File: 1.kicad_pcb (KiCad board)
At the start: 2 copper layers, 85.1 x 46.4 mm, 44 parts, among them J1 Micro_SD_Card, J10 I2C1, J11 I2C2, J12 B3..9A, J2 USB_B_Micro, J3 Conn_Power, J4 SWD, J5 Protected, J6 SPI1, J7 ADC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

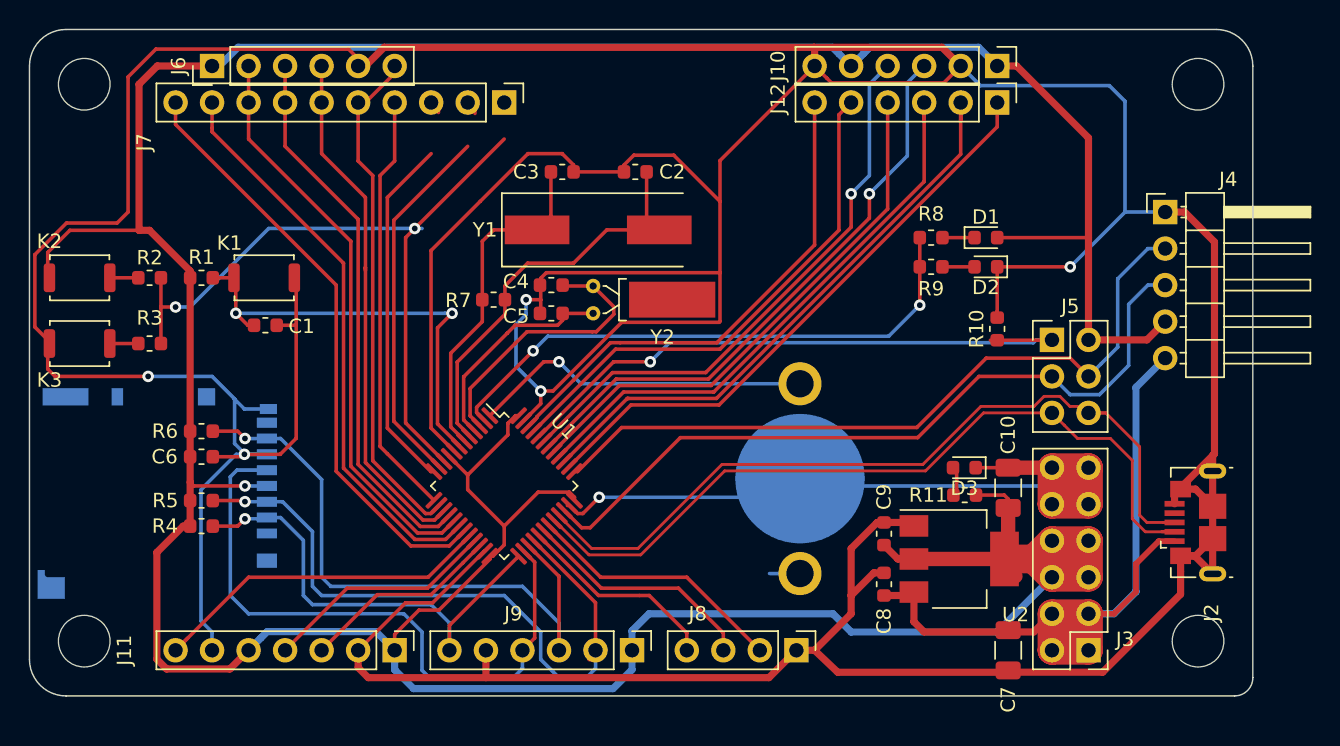
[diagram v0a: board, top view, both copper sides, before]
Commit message: operate line near edge
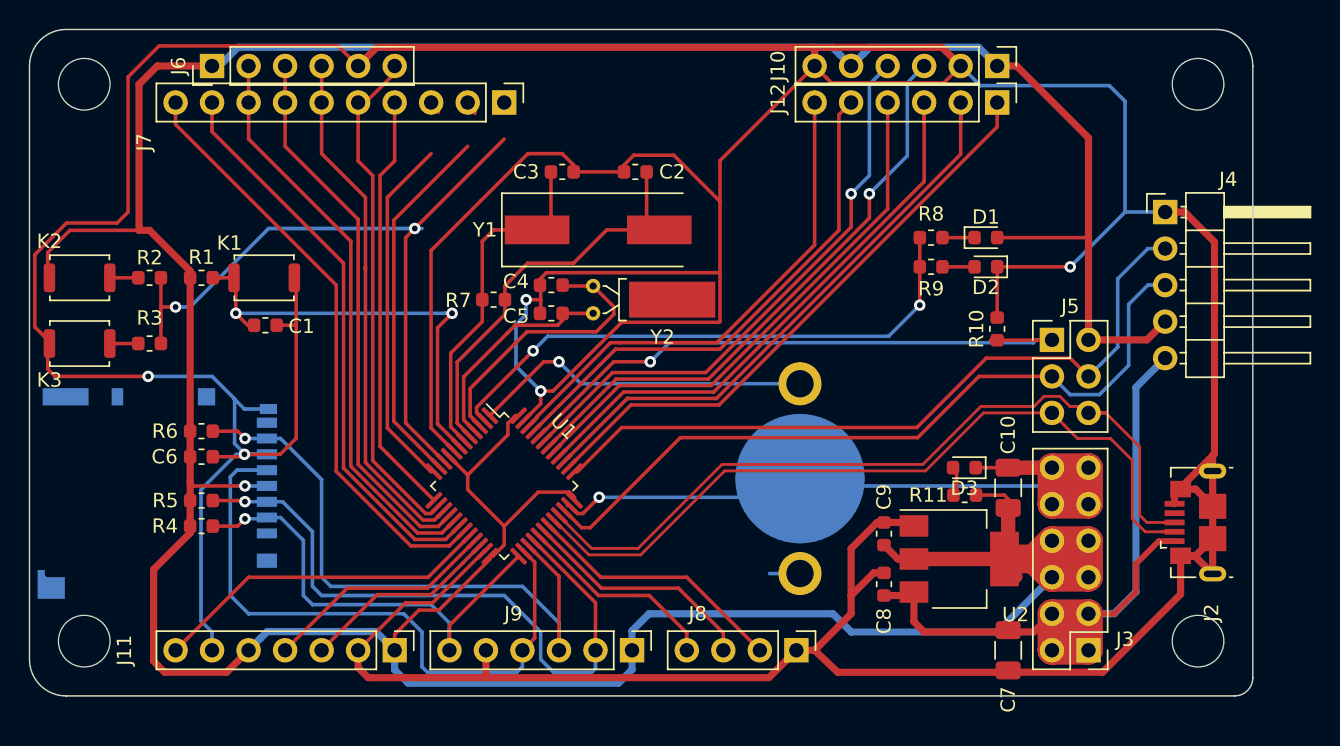
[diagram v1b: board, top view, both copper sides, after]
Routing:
- net /SD_SCLK: track 44.3 -> 43.8 mm

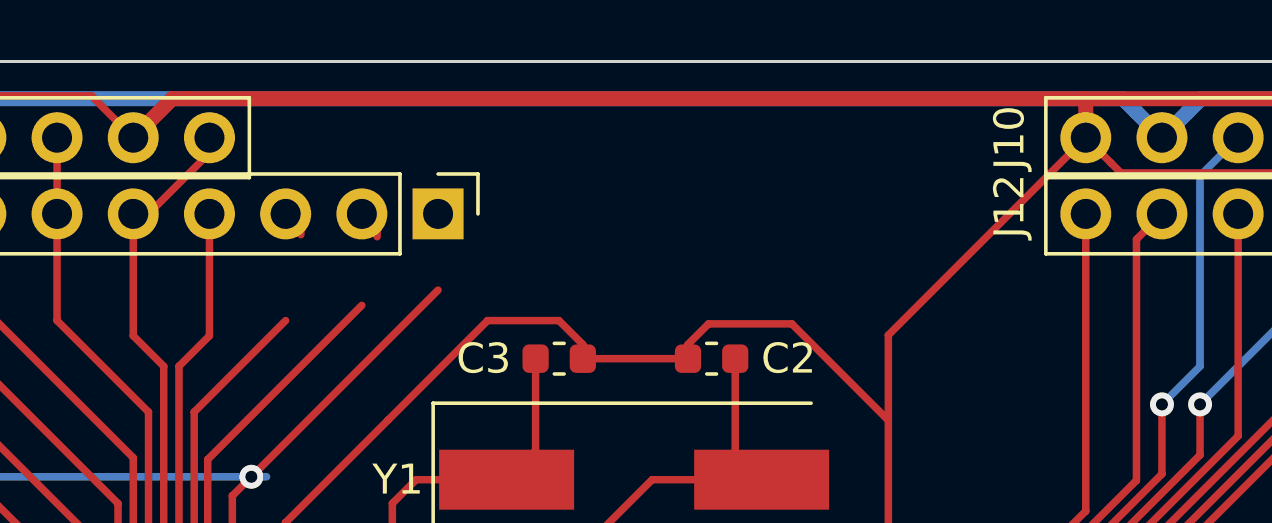
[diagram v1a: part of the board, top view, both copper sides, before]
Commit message: fix: ADC channel no connect
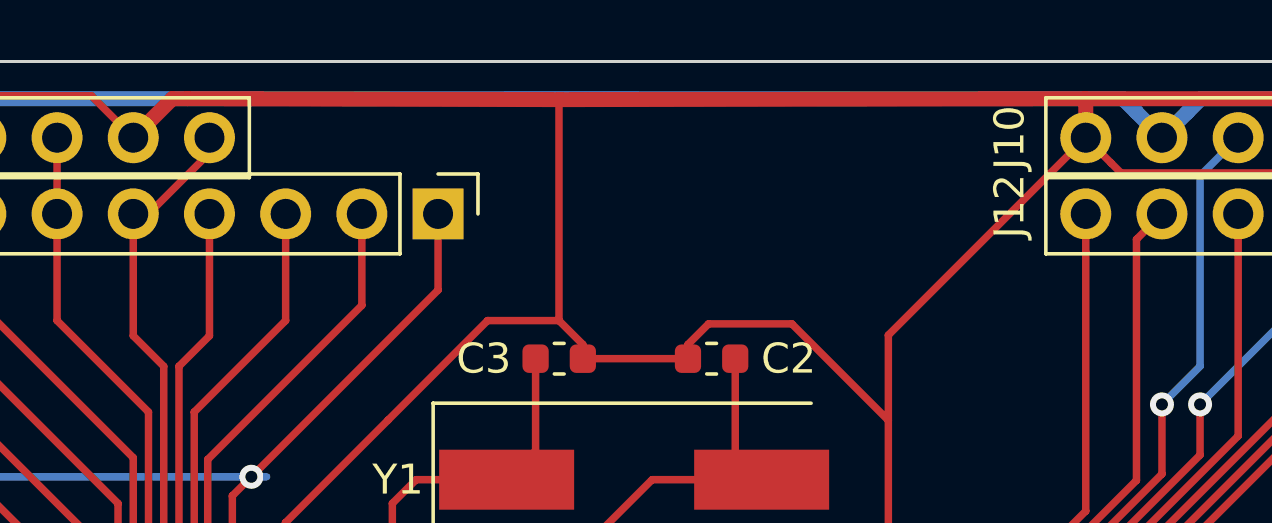
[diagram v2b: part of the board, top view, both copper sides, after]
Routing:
- net GND: track 485.7 -> 493.1 mm
- net /PA0: track 52.5 -> 55.0 mm
- net /PA2: track 26.0 -> 28.4 mm
- net /PA1: track 27.0 -> 28.7 mm
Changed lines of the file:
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@@
     (thickness 1.6)
     (drawings 27)
-    (tracks 644)
+    (tracks 648)
     (zones 0)
     (modules 44)
@@
       (effects (font (size 1 1) (thickness 0.15)))
     )
-    (fp_text value 8MHz (at 11.244 5.110244) (layer F.Fab) hide
+    (fp_text value 8MHz (at 9.212 0.030244) (layer F.Fab) hide
       (effects (font (size 1 1) (thickness 0.15)))
     )
@@
       (effects (font (size 1 1) (thickness 0.15)))
     )
-    (fp_text value 32.768k (at 5.7735 10.795) (layer F.Fab) hide
+    (fp_text value 32.768k (at 0.9475 12.104) (layer F.Fab) hide
       (effects (font (size 1 1) (thickness 0.15)))
     )
@@
     )
   )
-  (gr_text "ADCx\nCH9..0" (at 120.142 102.87) (layer Dwgs.User)
+  (gr_text "ADCx\nCH9..0" (at 120.142 109.4994) (layer Dwgs.User)
     (effects (font (size 1.5 1.5) (thickness 0.3)))
   )
@@
   (segment (start 159.989999 87.599999) (end 151.099999 87.599999) (width 0.5) (layer F.Cu) (net 7))
   (segment (start 161.29 88.9) (end 159.989999 87.599999) (width 0.5) (layer F.Cu) (net 7))
-  (segment (start 121.188001 87.599999) (end 151.099999 87.599999) (width 0.5) (layer F.Cu) (net 7))
   (segment (start 120.680001 87.599999) (end 121.188001 87.599999) (width 0.5) (layer F.Cu) (net 7))
   (segment (start 119.38 88.9) (end 120.680001 87.599999) (width 0.5) (layer F.Cu) (net 7))
@@
   (segment (start 98.298 110.49) (end 104.775 110.49) (width 0.25) (layer F.Cu) (net 7))
   (segment (start 119.38 88.9) (end 117.983 87.503) (width 0.25) (layer F.Cu) (net 7))
+  (segment (start 133.571 87.663) (end 133.604 87.63) (width 0.25) (layer F.Cu) (net 7))
+  (segment (start 133.571 94.996) (end 133.571 87.663) (width 0.25) (layer F.Cu) (net 7))
+  (segment (start 133.604 87.63) (end 151.099999 87.599999) (width 0.5) (layer F.Cu) (net 7))
+  (segment (start 121.188001 87.599999) (end 133.604 87.63) (width 0.5) (layer F.Cu) (net 7))
   (segment (start 163.83 100.838) (end 170.18 100.838) (width 0.25) (layer F.Cu) (net 8))
   (segment (start 170.18 100.838) (end 170.18 107.95) (width 0.5) (layer F.Cu) (net 8))
@@
   (segment (start 120.904 115.360664) (end 121.412 115.868664) (width 0.25) (layer F.Cu) (net 32))
   (segment (start 120.904 96.52) (end 120.904 115.360664) (width 0.25) (layer F.Cu) (net 32))
-  (segment (start 124.968 90.932) (end 124.968 92.134081) (width 0.25) (layer F.Cu) (net 33))
   (segment (start 124.46 94.996) (end 121.412 98.044) (width 0.25) (layer F.Cu) (net 33))
   (segment (start 124.439992 117.111212) (end 121.412 114.08322) (width 0.25) (layer F.Cu) (net 33))
   (segment (start 121.412 114.08322) (end 121.412 98.044) (width 0.25) (layer F.Cu) (net 33))
   (segment (start 124.652124 117.111212) (end 124.439992 117.111212) (width 0.25) (layer F.Cu) (net 33))
-  (segment (start 127.508 90.932) (end 127.508 92.202) (width 0.25) (layer F.Cu) (net 34))
+  (segment (start 124.46 91.44) (end 124.46 94.996) (width 0.25) (layer F.Cu) (net 33))
   (segment (start 121.86201 99.62599) (end 127 94.488) (width 0.25) (layer F.Cu) (net 34))
   (segment (start 121.86201 113.61399) (end 121.86201 99.62599) (width 0.25) (layer F.Cu) (net 34))
   (segment (start 125.005678 116.757658) (end 121.86201 113.61399) (width 0.25) (layer F.Cu) (net 34))
+  (segment (start 127 94.488) (end 127 91.44) (width 0.25) (layer F.Cu) (net 34))
   (segment (start 130.048 92.032) (end 130.048 90.932) (width 0.25) (layer F.Cu) (net 35))
   (segment (start 129.54 93.98) (end 123.317 100.203) (width 0.25) (layer F.Cu) (net 35))
@@
   (segment (start 122.682 113.726874) (end 122.682 100.838) (width 0.25) (layer F.Cu) (net 35))
   (segment (start 125.359231 116.404105) (end 122.682 113.726874) (width 0.25) (layer F.Cu) (net 35))
+  (segment (start 129.54 93.98) (end 129.54 91.44) (width 0.25) (layer F.Cu) (net 35))
   (segment (start 151.13 92.71) (end 151.13 91.44) (width 0.25) (layer F.Cu) (net 36))
   (segment (start 136.931833 108.14601) (end 137.600401 108.146009) (width 0.25) (layer F.Cu) (net 36))

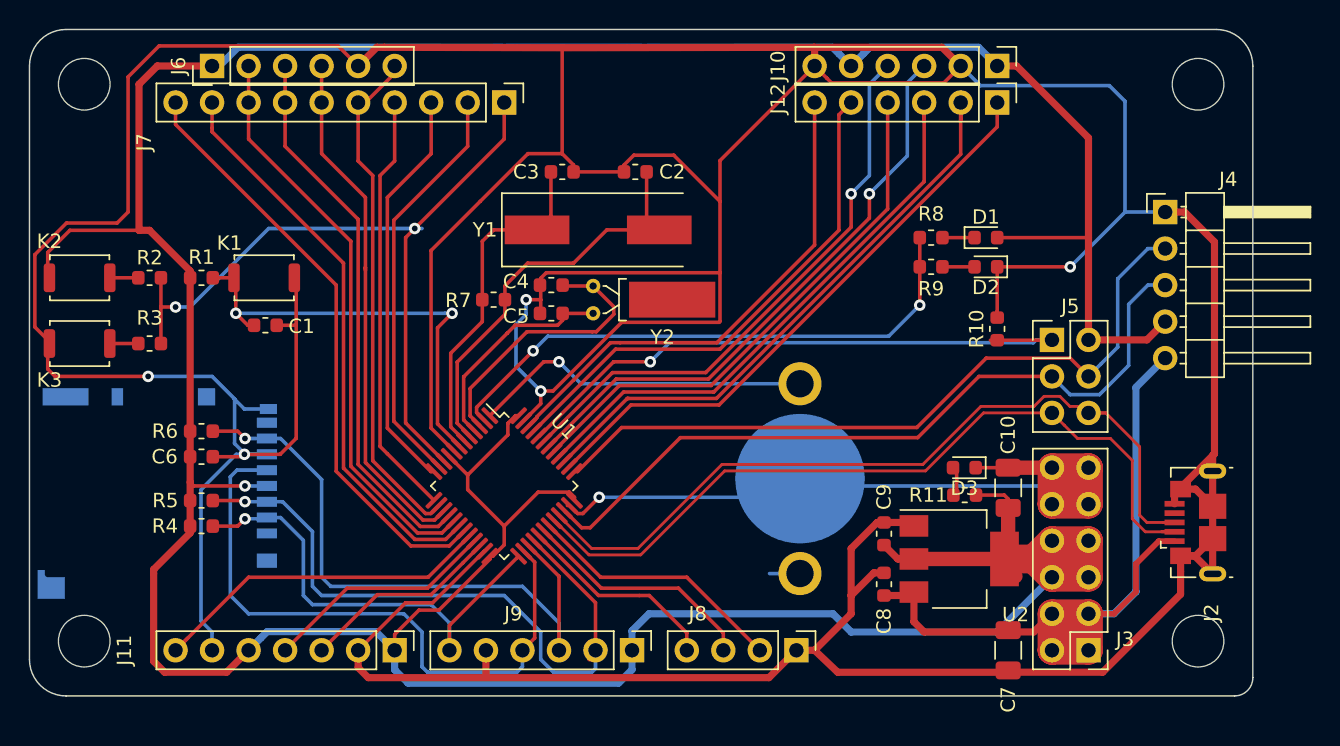
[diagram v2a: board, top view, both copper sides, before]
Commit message: label two colors
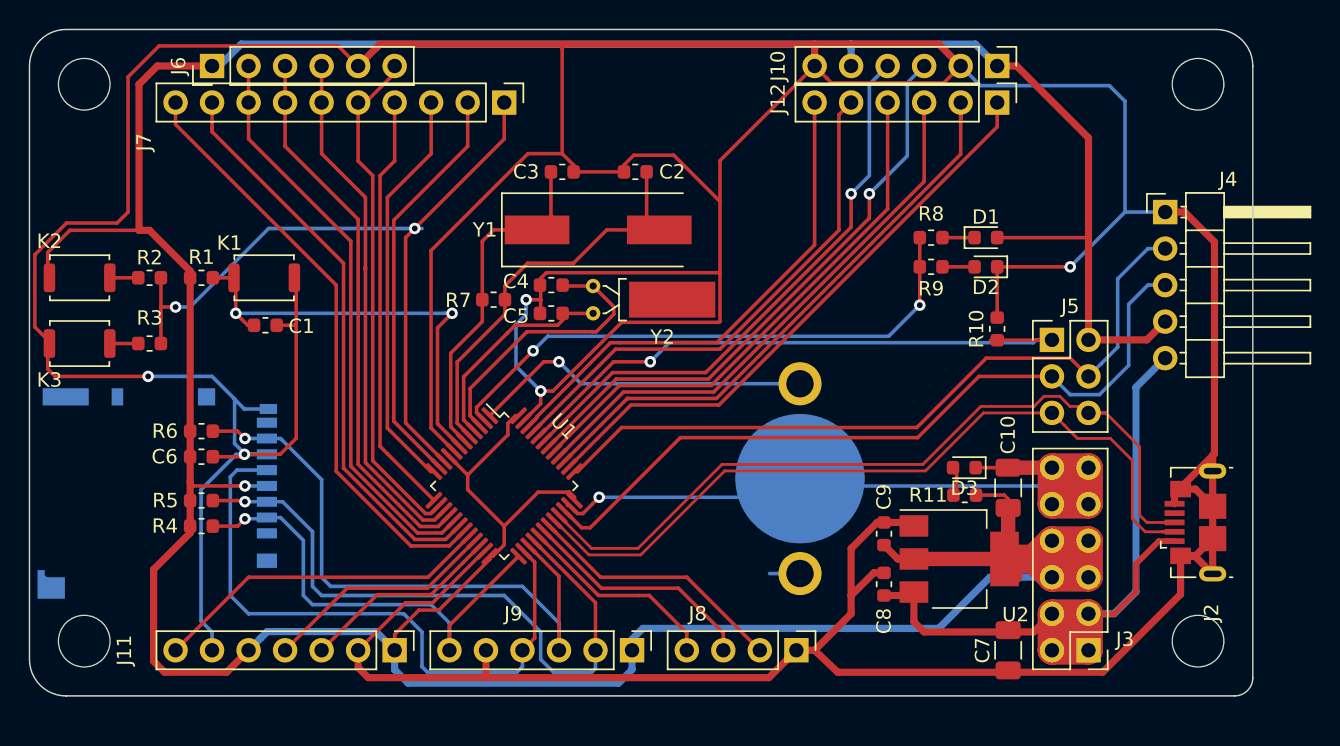
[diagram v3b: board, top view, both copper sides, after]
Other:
- board text added: "+ -"
- board text added: "- +"
- board text added: "- + SCL SDA - +"
- board text added: ". . . . SPI1"
- board text added: "2 1 2 1 TIM3 TIM4"
- board text added: "3V3 GND"
- board text added: "B11 B10 B2"
- board text added: "MOSI MISO SCK NSS"
- board text added: "OSC"
- board text added: "SDA SCL"
- board text added: "TIM4 2 1 4 3"
- board text removed: "- + SDA SCL - +"
- board text removed: "3V3 MOSI MISO SCK GND NSS"
- board text removed: "B11 B10"
- board text removed: "B2 - + SCL SDA - +"

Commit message: labels
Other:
- board text added: "- + - +"
- board text added: ". . I2C1"
- board text added: "2 1 TIM2"
- board text added: "2 1 TIM3"
- board text added: "GND"
- board text added: "GND 3V3"
- board text added: "GND 3V3 5V"
- board text added: "MCO Tx Rx"
- board text added: "NSS SCK MISO MOSI"
- board text added: "SCL SDA"
- board text added: "TIM1 1 2 3"
- board text added: "TIM2 3 4"
- board text added: "UART3 Tx Rx"
- board text removed: "+ -"
- board text removed: "- +"
- board text removed: "- + SCL SDA - +"
- board text removed: "2 1 2 1 TIM3 TIM4"
- board text removed: "MCO Tx Rx GND"
- board text removed: "NSS GND SCK MISO MOSI 3V3"
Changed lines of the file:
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@@
   (general
     (thickness 1.6)
-    (drawings 34)
+    (drawings 43)
     (tracks 645)
     (zones 0)
@@
   )
   (setup
-    (last_trace_width 0.5)
+    (last_trace_width 0.25)
     (user_trace_width 0.2)
     (user_trace_width 0.4)
@@
       (effects (font (size 1 1) (thickness 0.15)))
     )
-    (fp_text value UART1 (at -2.54 3.175 180) (layer F.Fab)
+    (fp_text value UART1 (at 0 -4.572 180) (layer F.Fab)
       (effects (font (size 1 1) (thickness 0.15)))
     )
@@
       (effects (font (size 1 1) (thickness 0.15)))
     )
-    (fp_text value 20p (at 5.334 0.254) (layer F.Fab) hide
+    (fp_text value 20p (at 0.6095 2.159) (layer F.Fab) hide
       (effects (font (size 1 1) (thickness 0.15)))
     )
@@
     )
   )
-  (gr_text "2  1  2  1\nTIM3  TIM4" (at 147.32 90.805) (layer Eco2.User)
+  (gr_text "TIM1\n1  2  3" (at 144.78 126.492) (layer Eco2.User)
+    (effects (font (size 1 1) (thickness 0.15)))
+  )
+  (gr_text "TIM2   3   4" (at 113.284 122.174) (layer Eco2.User)
+    (effects (font (size 0.8 0.8) (thickness 0.15)))
+  )
+  (gr_text ".  .  .  .\nSPI1" (at 115.824 99.314) (layer Eco1.User)
+    (effects (font (size 1.25 1.25) (thickness 0.2)))
+  )
+  (gr_text "UART3  Tx  Rx" (at 113.284 123.444) (layer Eco1.User)
+    (effects (font (size 0.8 0.8) (thickness 0.15)))
+  )
+  (gr_text ".  .\nI2C1" (at 152.527 97.028) (layer Eco2.User)
+    (effects (font (size 1.25 1.25) (thickness 0.2)))
+  )
+  (gr_text "2  1\nTIM2" (at 146.812 90.932) (layer Eco1.User)
+    (effects (font (size 0.8 0.8) (thickness 0.15)) (justify right))
+  )
+  (gr_text "GND\n\n\n3V3\n\n\n5V" (at 172.847 123.19) (layer Eco2.User)
+    (effects (font (size 1.1 1.1) (thickness 0.2)))
+  )
+  (gr_text GND (at 149.86 131.445) (layer Eco2.User)
+    (effects (font (size 0.65 0.65) (thickness 0.15)))
+  )
+  (gr_text "-   +           -   +" (at 157.48 87.122) (layer Eco2.User)
+    (effects (font (size 0.8 0.8) (thickness 0.2)))
+  )
+  (gr_text "GND                 3V3" (at 133.35 131.445) (layer Eco2.User)
+    (effects (font (size 0.65 0.65) (thickness 0.15)))
+  )
+  (gr_text "-   +           -   +" (at 115.57 131.318) (layer Eco2.User)
+    (effects (font (size 0.8 0.8) (thickness 0.2)))
+  )
+  (gr_text "2  1\nTIM3" (at 143.256 90.932) (layer Eco2.User)
     (effects (font (size 0.8 0.8) (thickness 0.15)) (justify right))
   )
@@
     (effects (font (size 0.65 0.65) (thickness 0.15)))
   )
-  (gr_text "+  -" (at 152.4 87.122) (layer Eco2.User)
-    (effects (font (size 1 1) (thickness 0.15)))
-  )
-  (gr_text "-  +" (at 162.56 87.122) (layer Eco2.User)
-    (effects (font (size 1 1) (thickness 0.15)))
-  )
   (gr_text "TIM4  2  1\n4  3" (at 136.525 89.535) (layer Eco1.User)
     (effects (font (size 0.8 0.8) (thickness 0.15)) (justify left))
   )
-  (gr_text ".  .  .  .\nSPI1" (at 159.766 97.028) (layer Dwgs.User)
-    (effects (font (size 1 1) (thickness 0.15)))
+  (gr_text ".  .  .  .\nSPI1" (at 160.147 97.028) (layer Eco1.User)
+    (effects (font (size 1.25 1.25) (thickness 0.2)))
   )
   (gr_text OSC (at 127 109.982) (layer Dwgs.User)
     (effects (font (size 1 1) (thickness 0.15)))
   )
-  (gr_text "-    +  SCL  SDA  -    +" (at 115.57 131.318) (layer Dwgs.User)
+  (gr_text "SCL  SDA" (at 115.57 131.445) (layer Eco1.User)
     (effects (font (size 0.65 0.65) (thickness 0.15)))
   )
@@
     (effects (font (size 1.2 1.2) (thickness 0.2)))
   )
-  (gr_text SWD (at 149.86 114.3) (layer Dwgs.User)
+  (gr_text SWD (at 149.86 114.3) (layer Eco1.User)
     (effects (font (size 1.5 1.5) (thickness 0.3)))
   )
-  (gr_text USB (at 149.86 116.84) (layer Dwgs.User)
+  (gr_text USB (at 149.86 116.84) (layer Eco1.User)
     (effects (font (size 1.5 1.5) (thickness 0.3)))
   )
@@
   (gr_line (start 96.52 130.175) (end 96.52 88.9) (layer Edge.Cuts) (width 0.1))
   (gr_line (start 180.34 132.715) (end 99.06 132.715) (layer Edge.Cuts) (width 0.1))
-  (gr_text "MCO  Tx  Rx  GND" (at 146.05 131.318) (layer Dwgs.User)
+  (gr_text "MCO  Tx   Rx" (at 144.653 131.445) (layer Eco1.User)
     (effects (font (size 0.65 0.65) (thickness 0.15)))
   )
-  (gr_text "NSS GND SCK MISO MOSI 3V3" (at 132.08 131.318) (layer Dwgs.User)
+  (gr_text "NSS     SCK MISO MOSI" (at 131.064 131.445) (layer Eco1.User)
     (effects (font (size 0.65 0.65) (thickness 0.15)))
   )
@@
     (effects (font (size 1.55 1.55) (thickness 0.25)) (justify left))
   )
-  (gr_text "Tx Rx\nUART2" (at 123.19 97.282) (layer Dwgs.User)
-    (effects (font (size 0.8 1) (thickness 0.15)))
+  (gr_text "Tx Rx\nUART2" (at 123.571 99.695) (layer Eco1.User)
+    (effects (font (size 1 1) (thickness 0.15)))
   )
   (gr_text "A0\nA1\nA2\nA3\nA4\nA5\nA6\nA7\nB0\nB1" (at 118.237 93.98 270) (layer Dwgs.User)
     (effects (font (size 1.5 1.5) (thickness 0.3)))
   )
-  (gr_text "4  3  2  1\nTIM2" (at 130.175 96.52) (layer Dwgs.User)
-    (effects (font (size 0.8 1) (thickness 0.15)) (justify right))
-  )
-  (gr_text "4  3  2  1\nTIM3" (at 110.617 96.52) (layer Dwgs.User)
-    (effects (font (size 0.8 1) (thickness 0.15)))
+  (gr_text "4  3  2  1\nTIM2" (at 126.111 96.901) (layer Eco2.User)
+    (effects (font (size 1 1) (thickness 0.15)))
+  )
+  (gr_text "4  3  2  1\nTIM3" (at 110.617 96.901) (layer Eco2.User)
+    (effects (font (size 1 1) (thickness 0.15)))
   )
   (segment (start 135.656008 130.192212) (end 135.443876 130.192212) (width 0.25) (layer F.Cu) (net 1))
@@
   (segment (start 119.38 91.44) (end 119.38 95.504) (width 0.25) (layer F.Cu) (net 26))
   (segment (start 119.888 102.917456) (end 119.888 103.124) (width 0.25) (layer F.Cu) (net 27))
-  (segment (start 114.3 88.9) (end 114.3 91.44) (width 0.25) (layer F.Cu) (net 28))
   (segment (start 119.888 102.917456) (end 119.854467 102.950989) (width 0.25) (layer F.Cu) (net 27))
   (segment (start 124.694828 120.480298) (end 125.359231 119.815895) (width 0.25) (layer F.Cu) (net 27))
@@
   (segment (start 116.84 91.44) (end 116.84 94.996) (width 0.25) (layer F.Cu) (net 27))
   (segment (start 116.84 88.9) (end 116.84 91.44) (width 0.25) (layer F.Cu) (net 27))
+  (segment (start 114.3 88.9) (end 114.3 91.44) (width 0.25) (layer F.Cu) (net 28))
   (segment (start 124.951926 120.930308) (end 125.712785 120.169449) (width 0.25) (layer F.Cu) (net 28))
   (segment (start 123.698206 120.930308) (end 124.951926 120.930308) (width 0.25) (layer F.Cu) (net 28))
